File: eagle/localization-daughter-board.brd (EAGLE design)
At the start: 65 x 30 mm, 23 parts, among them J1 MOLEX-22-03-5035, U1 TXS0101DCKR, U2 RPI-ZERO, U3 LM1085ISX-ADJ, U4 EXB-38V121JV, U5 STM32F042FXP

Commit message: Current design
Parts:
- renumbered LED1 to STAT1, LED2 to STAT2, LED3 to DYN, LED4 to I2C
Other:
- board text added: "PB1"

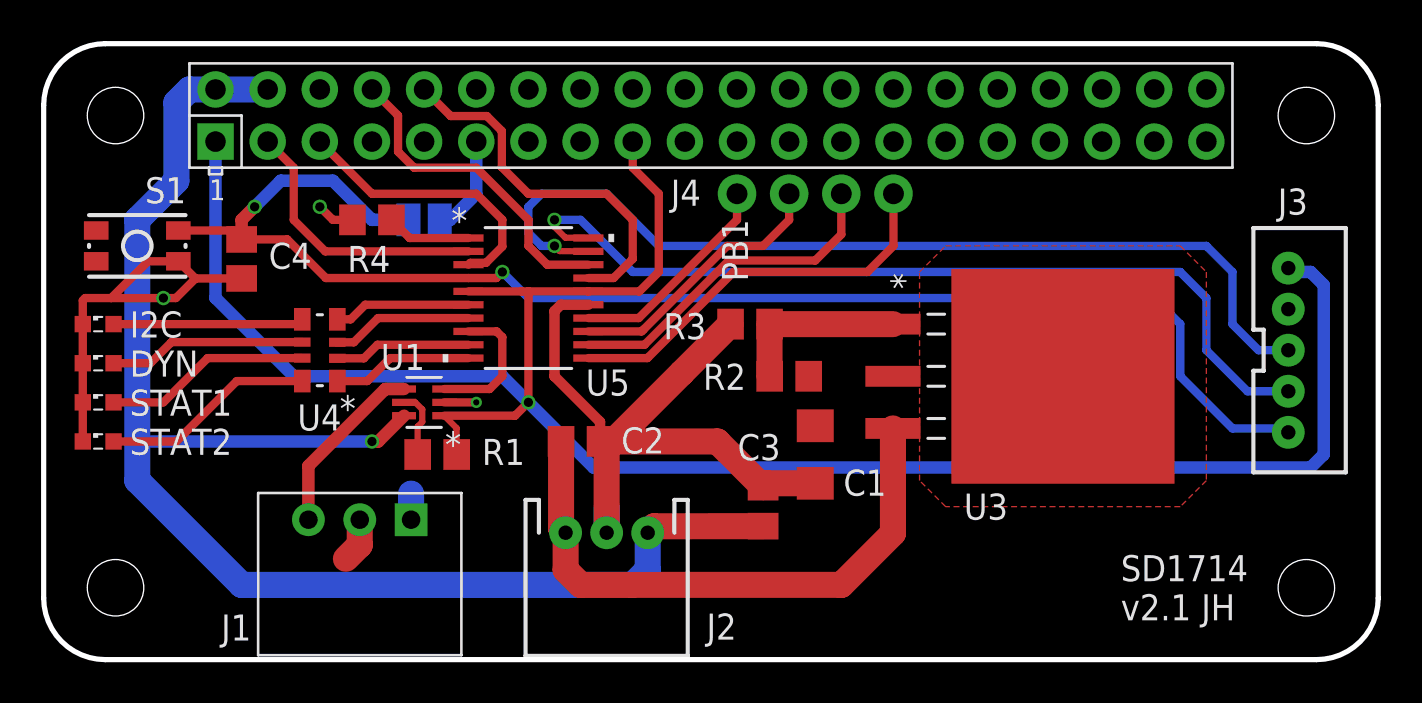
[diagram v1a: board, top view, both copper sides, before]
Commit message: Added additional capacitors
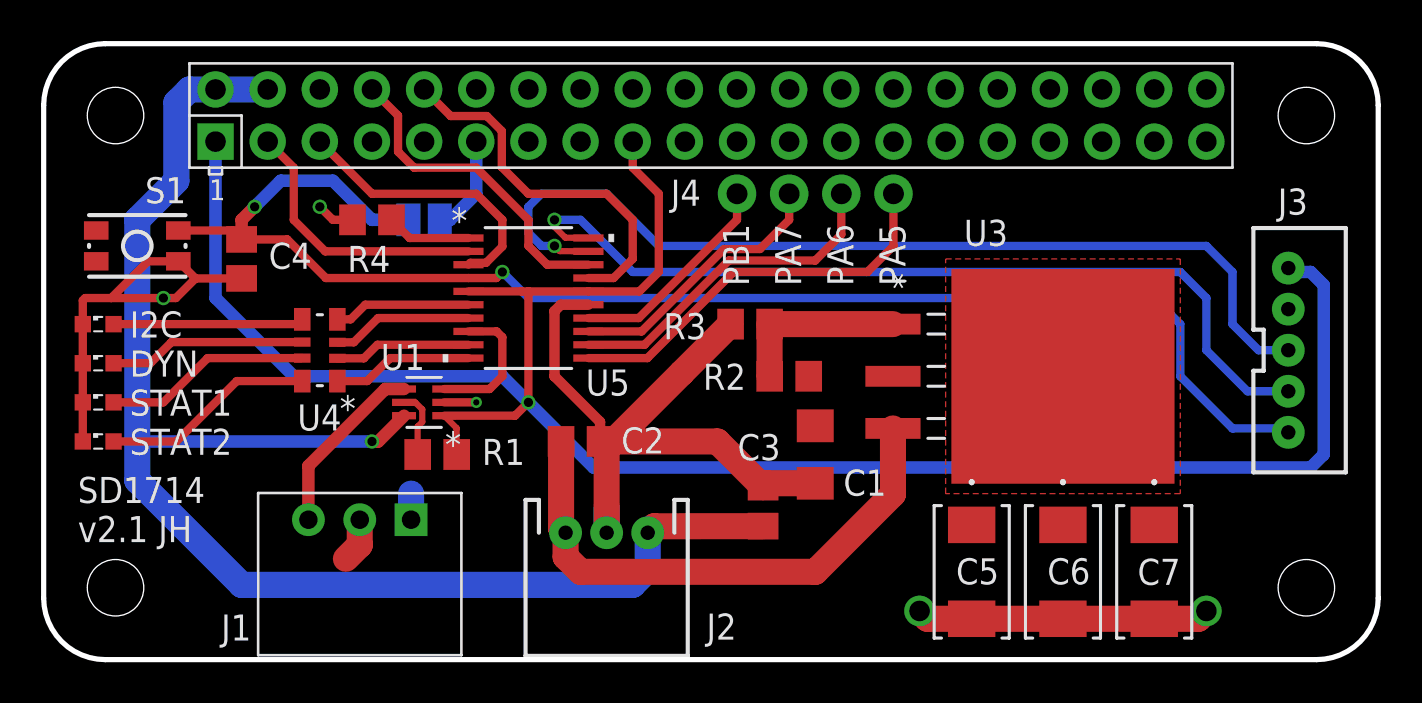
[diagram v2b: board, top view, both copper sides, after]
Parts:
- added C5, C6, C7: F931C107MCC, Localization-Daughter-Board:F93-C
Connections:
- net +10V: now also C5.1, C6.1, C7.1
- net GND: now also C5.2, C6.2, C7.2
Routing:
- net GND: track 60.2 -> 74.5 mm, vias 3 -> 5
- net +12V: track 28.7 -> 26.7 mm
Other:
- board text added: "PA5"
- board text added: "PA6"
- board text added: "PA7"
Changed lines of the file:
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@@
 <setting verticaltext="up"/>
 </settings>
-<grid distance="50" unitdist="mil" unit="mil" style="lines" multiple="1" display="yes" altdistance="1" altunitdist="mil" altunit="mil"/>
+<grid distance="50" unitdist="mil" unit="mil" style="lines" multiple="1" display="yes" altdistance="25" altunitdist="mil" altunit="mil"/>
 <layers>
 <layer number="1" name="Top" color="4" fill="1" visible="yes" active="yes"/>
@@
 <wire x1="62.52" y1="30.17" x2="3.52" y2="30.17" width="0.254" layer="20"/>
 <wire x1="3.52" y1="30.17" x2="0.52" y2="27.17" width="0.254" layer="20" curve="90"/>
-<text x="52.9844" y="2.0828" size="1.27" layer="25" font="vector">SD1714
+<text x="2.1844" y="5.8928" size="1.27" layer="25" font="vector">SD1714
 v2.1 JH</text>
-<text x="34.8234" y="18.5928" size="1.27" layer="25" font="vector" rot="R90">PB1</text>
+<text x="33.6042" y="21.3868" size="1.27" layer="25" font="vector" rot="R270">PB1</text>
+<text x="36.1442" y="21.3868" size="1.27" layer="25" font="vector" rot="R270">PA7</text>
+<text x="38.6842" y="21.3868" size="1.27" layer="25" font="vector" rot="R270">PA6</text>
+<text x="41.2242" y="21.3868" size="1.27" layer="25" font="vector" rot="R270">PA5</text>
 </plain>
 <attributes>
@@
 <element name="U3" library="bbb_localization_cape" library_urn="urn:adsk.eagle:library:616562" package="TS3B" package3d_urn="urn:adsk.eagle:package:616615/2" value="LM1085ISX-ADJ" x="50.165" y="13.97" smashed="yes" rot="R270">
 <attribute name="MANUFACTURER_PART_NUMBER" value="lm1085isxadj" x="50.165" y="13.97" size="1.778" layer="27" rot="R270" display="off"/>
-<attribute name="NAME" x="45.339" y="6.985" size="1.27" layer="25" font="vector" rot="SR0"/>
+<attribute name="NAME" x="45.339" y="20.32" size="1.27" layer="25" font="vector" rot="SR0"/>
 <attribute name="VENDOR" value="Texas Instruments" x="50.165" y="13.97" size="1.778" layer="27" rot="R270" display="off"/>
 </element>
@@
 <attribute name="PROD_ID" value="CONN-09696" x="34.29" y="22.86" size="1.778" layer="27" display="off"/>
 <attribute name="VALUE" x="33.02" y="20.828" size="0.6096" layer="27" font="vector" ratio="20"/>
+</element>
+<element name="C5" library="Localization-Daughter-Board" library_urn="urn:adsk.eagle:library:1230207" package="F93-C" package3d_urn="urn:adsk.eagle:package:1231828/1" value="F931C107MCC" x="45.72" y="4.445" smashed="yes" rot="R270">
+<attribute name="MANUFACTURER_PART_NUMBER" value="F931C107MCC" x="45.72" y="4.445" size="1.778" layer="27" rot="R270" display="off"/>
+<attribute name="NAME" x="44.958" y="3.8354" size="1.27" layer="25" font="vector" rot="SR0"/>
+<attribute name="VENDOR" value="AVX Corporation" x="45.72" y="4.445" size="1.778" layer="27" rot="R270" display="off"/>
+</element>
+<element name="C6" library="Localization-Daughter-Board" library_urn="urn:adsk.eagle:library:1230207" package="F93-C" package3d_urn="urn:adsk.eagle:package:1231828/1" value="F931C107MCC" x="50.165" y="4.445" smashed="yes" rot="R270">
+<attribute name="MANUFACTURER_PART_NUMBER" value="F931C107MCC" x="50.165" y="4.445" size="1.778" layer="27" rot="R270" display="off"/>
+<attribute name="NAME" x="49.403" y="3.8354" size="1.27" layer="25" font="vector" rot="SR0"/>
+<attribute name="VENDOR" value="AVX Corporation" x="50.165" y="4.445" size="1.778" layer="27" rot="R270" display="off"/>
+</element>
+<element name="C7" library="Localization-Daughter-Board" library_urn="urn:adsk.eagle:library:1230207" package="F93-C" package3d_urn="urn:adsk.eagle:package:1231828/1" value="F931C107MCC" x="54.61" y="4.445" smashed="yes" rot="R270">
+<attribute name="MANUFACTURER_PART_NUMBER" value="F931C107MCC" x="54.61" y="4.445" size="1.778" layer="27" rot="R270" display="off"/>
+<attribute name="NAME" x="53.7972" y="3.81" size="1.27" layer="25" font="vector" rot="SR0"/>
+<attribute name="VENDOR" value="AVX Corporation" x="54.61" y="4.445" size="1.778" layer="27" rot="R270" display="off"/>
 </element>
 </elements>
@@
 <wire x1="25.4" y1="13.97" x2="27.62" y2="11.75" width="0.508" layer="1"/>
 <wire x1="27.62" y1="11.75" x2="27.62" y2="10.795" width="0.508" layer="1"/>
+<contactref element="C5" pad="2"/>
+<contactref element="C6" pad="2"/>
+<contactref element="C7" pad="2"/>
+<wire x1="45.72" y1="2.159" x2="50.165" y2="2.159" width="1.27" layer="1"/>
+<wire x1="50.165" y1="2.159" x2="54.61" y2="2.159" width="1.27" layer="1"/>
+<via x="43.18" y="2.54" extent="1-16" drill="1"/>
+<via x="57.15" y="2.54" extent="1-16" drill="1"/>
+<wire x1="45.72" y1="2.159" x2="43.561" y2="2.159" width="1.27" layer="1"/>
+<wire x1="43.561" y1="2.159" x2="43.18" y2="2.54" width="1.27" layer="1"/>
+<wire x1="54.61" y1="2.159" x2="56.769" y2="2.159" width="1.27" layer="1"/>
+<wire x1="56.769" y1="2.159" x2="57.15" y2="2.54" width="1.27" layer="1"/>
 </signal>
 <signal name="+12V">
@@
 <wire x1="25.72" y1="10.795" x2="25.72" y2="6.57" width="1.27" layer="1"/>
 <wire x1="25.72" y1="6.57" x2="25.94" y2="6.35" width="1.27" layer="1"/>
-<wire x1="25.94" y1="6.35" x2="25.94" y2="4.54" width="1.27" layer="1"/>
-<wire x1="25.94" y1="4.54" x2="26.67" y2="3.81" width="1.27" layer="1"/>
-<wire x1="26.67" y1="3.81" x2="39.37" y2="3.81" width="1.27" layer="1"/>
-<wire x1="39.37" y1="3.81" x2="41.8846" y2="6.3246" width="1.27" layer="1"/>
-<wire x1="41.8846" y1="6.3246" x2="41.8846" y2="11.43" width="1.27" layer="1"/>
+<wire x1="25.94" y1="6.35" x2="25.94" y2="5.175" width="1.27" layer="1"/>
+<wire x1="25.94" y1="5.175" x2="26.67" y2="4.445" width="1.27" layer="1"/>
+<wire x1="26.67" y1="4.445" x2="38.1" y2="4.445" width="1.27" layer="1"/>
+<wire x1="38.1" y1="4.445" x2="41.8846" y2="8.2296" width="1.27" layer="1"/>
+<wire x1="41.8846" y1="8.2296" x2="41.8846" y2="11.43" width="1.27" layer="1"/>
 </signal>
 <signal name="+5V">
@@
 <contactref element="J1" pad="P$2"/>
 <polygon width="0.2032" layer="1" thermals="no" rank="2">
-<vertex x="44.45" y="20.32"/>
-<vertex x="55.88" y="20.32"/>
-<vertex x="57.15" y="19.05"/>
-<vertex x="57.15" y="8.89"/>
-<vertex x="55.88" y="7.62"/>
-<vertex x="44.45" y="7.62"/>
-<vertex x="43.18" y="8.89"/>
-<vertex x="43.18" y="19.05"/>
+<vertex x="44.45" y="19.685"/>
+<vertex x="55.88" y="19.685"/>
+<vertex x="55.88" y="8.255"/>
+<vertex x="44.45" y="8.255"/>
 </polygon>
 <wire x1="15.915" y1="6.985" x2="15.915" y2="5.755" width="1.27" layer="1"/>
 <wire x1="15.915" y1="5.755" x2="15.24" y2="5.08" width="1.27" layer="1"/>
+<contactref element="C5" pad="1"/>
+<contactref element="C6" pad="1"/>
+<contactref element="C7" pad="1"/>
 </signal>
 <signal name="DYN_DATA">
@@
 <contactref element="J4" pad="2"/>
 <contactref element="U5" pad="13"/>
-<wire x1="29.73646875" y1="16.24619375" x2="33.810275" y2="20.32" width="0.4064" layer="1"/>
-<wire x1="35.56" y1="20.32" x2="36.83" y2="21.59" width="0.4064" layer="1"/>
+<wire x1="27.051" y1="16.155" x2="29.64526875" y2="16.155" width="0.4064" layer="1"/>
+<wire x1="35.4076" y1="20.1676" x2="36.83" y2="21.59" width="0.4064" layer="1"/>
+<wire x1="29.64526875" y1="16.155" x2="33.65786875" y2="20.1676" width="0.4064" layer="1"/>
+<wire x1="33.65786875" y1="20.1676" x2="35.4076" y2="20.1676" width="0.4064" layer="1"/>
 <wire x1="36.83" y1="21.59" x2="36.83" y2="22.86" width="0.4064" layer="1"/>
-<wire x1="33.810275" y1="20.32" x2="35.56" y2="20.32" width="0.4064" layer="1"/>
-<wire x1="27.051" y1="16.155" x2="29.64526875" y2="16.155" width="0.4064" layer="1"/>
-<wire x1="29.64526875" y1="16.155" x2="29.7364625" y2="16.24619375" width="0.4064" layer="1"/>
-<wire x1="29.7364625" y1="16.24619375" x2="29.73646875" y2="16.24619375" width="0" layer="19" extent="1-1"/>
 </signal>
 <signal name="N$9">
